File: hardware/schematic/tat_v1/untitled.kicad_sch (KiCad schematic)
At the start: 30 parts, among them J1 JST-PH 2 Pin, J2 USB_C_Receptacle_USB2.0_14P, SW1 SW_SPDT, U1 BQ25185, U2 USBLC6-2P6, U3 TPS631000DRLR

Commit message: Finished all footprints, can now start laying out circuit
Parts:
- F1: footprint (none) -> tat_footprints:Littelfuse_0805L_Polyfuse
- J1: footprint (none) -> Connector_JST:JST_PH_S2B-PH-SM4-TB_1x02-1MP_P2.00mm_Horizontal; Link (none) -> https://www.lcsc.com/product-detail/Wire-To-Board-Connector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
- SW1: footprint (none) -> tat_footprints:SW_SPDT_HANXIA_Mini_MSK12CO2; Link (none) -> https://www.lcsc.com/product-detail/Slide-Switches_SHOU-HAN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
- U1: footprint (none) -> tat_footprints:WSON-10 BQ25185
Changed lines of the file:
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@@
 			)
 		)
-		(property "Footprint" ""
+		(property "Footprint" "tat_footprints:WSON-10 BQ25185"
 			(at 74.93 146.05 0)
 			(effects
@@
 			)
 		)
-		(property "Footprint" ""
+		(property "Footprint" "tat_footprints:SW_SPDT_HANXIA_Mini_MSK12CO2"
 			(at 212.09 142.24 0)
 			(effects
@@
 			)
 		)
-		(property "Datasheet" "~"
+		(property "Datasheet" "https://www.lcsc.com/datasheet/lcsc_datasheet_2407161403_SHOU-HAN-MINI-MSK12CO2_C2681570.pdf"
 			(at 212.09 134.62 0)
 			(effects
@@
 		)
 		(property "Description" "Switch, single pole double throw"
+			(at 212.09 142.24 0)
+			(effects
+				(font
+					(size 1.27 1.27)
+				)
+				(hide yes)
+			)
+		)
+		(property "Link" "https://www.lcsc.com/product-detail/Slide-Switches_SHOU-HAN-MINI-MSK12CO2_C2681570.html"
 			(at 212.09 142.24 0)
 			(effects
@@
 			)
 		)
-		(property "Footprint" ""
+		(property "Footprint" "tat_footprints:Littelfuse_0805L_Polyfuse"
 			(at 170.18 43.18 0)
 			(effects
@@
 			)
 		)
-		(property "Footprint" ""
+		(property "Footprint" "Connector_JST:JST_PH_S2B-PH-SM4-TB_1x02-1MP_P2.00mm_Horizontal"
 			(at 30.48 120.65 0)
 			(effects
@@
 			)
 		)
-		(property "Datasheet" "~"
+		(property "Datasheet" "https://www.lcsc.com/datasheet/lcsc_datasheet_2411192313_XUNPU-WAFER-PH2-0-2PWB_C3029440.pdf"
 			(at 30.48 120.65 0)
 			(effects
@@
 			)
 		)
-		(property "Description" "Generic connector, single row, 01x02, script generated"
+		(property "Description" "JST-PH 2-pin surface mount connector, right angle"
 			(at 30.48 120.65 0)
 			(effects
+				(font
+					(size 1.27 1.27)
+				)
+				(hide yes)
+			)
+		)
+		(property "Link" "https://www.lcsc.com/product-detail/Wire-To-Board-Connector_XUNPU-WAFER-PH2-0-2PWB_C3029440.html?s_z=n_XUNPU%2520WAFER-PH2.0-2PWB"
+			(at 30.48 120.65 0)
+			(effects

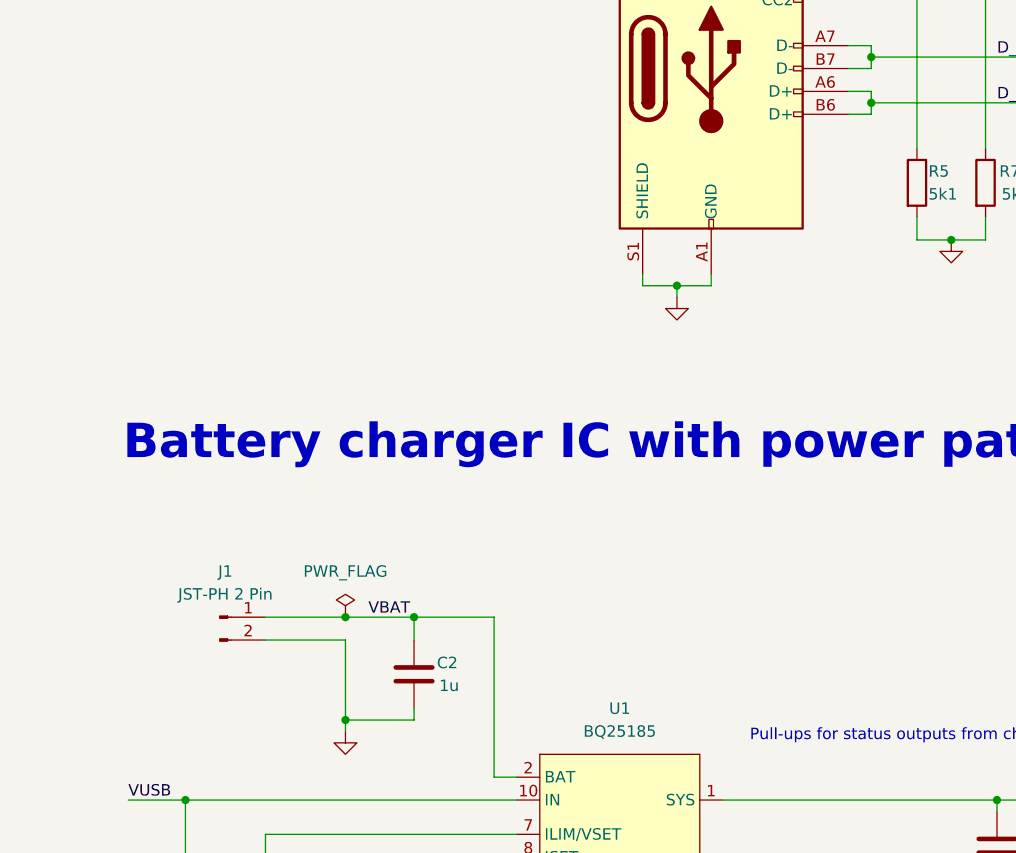
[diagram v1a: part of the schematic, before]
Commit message: Fixed all footprint-symbol mismatches, ready to start routing!
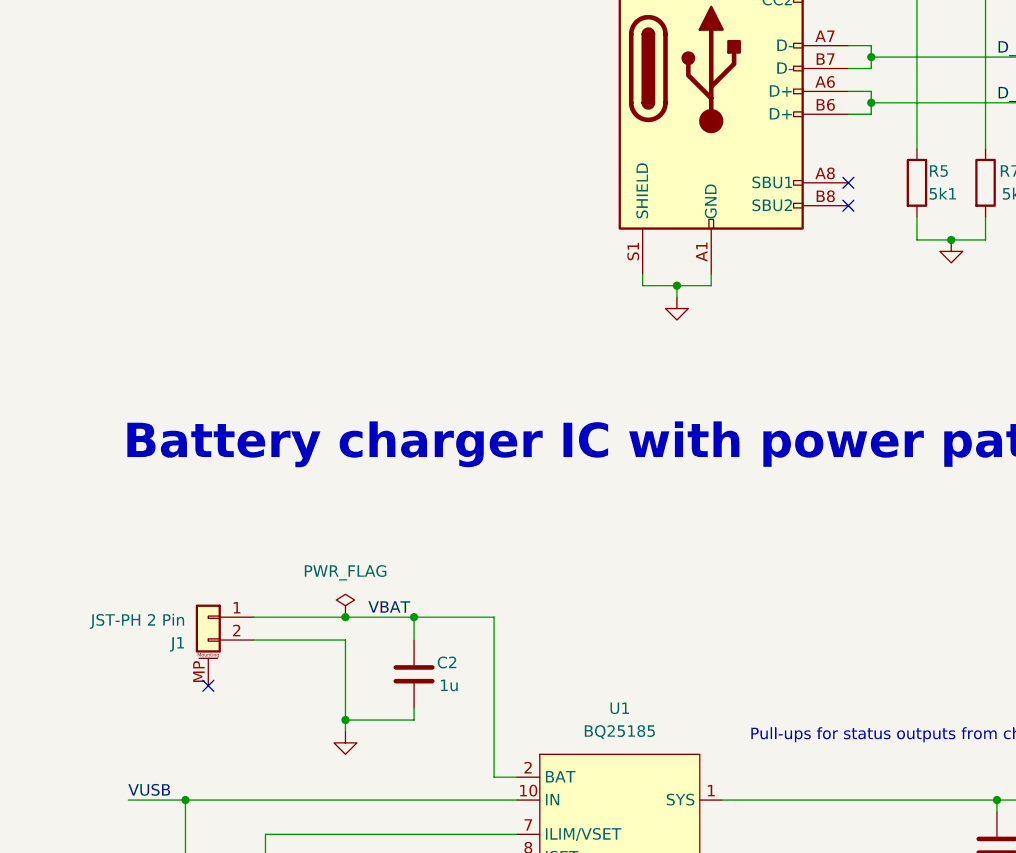
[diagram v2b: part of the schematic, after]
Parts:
- J1: symbol Connector:Conn_01x02_Pin -> Connector_Generic_MountingPin:Conn_01x02_MountingPin
- J2: symbol Connector:USB_C_Receptacle_USB2.0_14P -> Connector:USB_C_Receptacle_USB2.0_16P
- SW1: symbol Switch:SW_SPDT -> tat_library:MINI_MSK12CO2; Link https://www.lcsc.com/product-detail/Slide-Switches_SHOU-HAN-MINI-MSK12CO2_C2681570.html -> https://www.lcsc.com/product-detail/Slide-Switches_SHOU-HAN-MINI-MSK12CO2_C2681570.html?s_z=n_SHOU%2520HAN%2520MINI%2520MSK12CO2
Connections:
- no-connect marks 0 -> 3
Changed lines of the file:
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@@
 	)
 	(junction
+		(at 44.45 120.65)
+		(diameter 0)
+		(color 0 0 0 0)
+	)
+	(junction
 		(at 35.56 161.29)
 		(diameter 0)
@@
 	)
 	(junction
-		(at 44.45 120.65)
-		(diameter 0)
-		(color 0 0 0 0)
-	)
-	(junction
 		(at 44.45 132.08)
 		(diameter 0)
@@
 		(color 0 0 0 0)
 	)
+	(no_connect
+		(at 100.33 72.39)
+	)
+	(no_connect
+		(at 29.21 128.27)
+	)
+	(no_connect
+		(at 100.33 74.93)
+	)
 	(wire
 		(pts
@@
 	(wire
 		(pts
-			(xy 35.56 123.19) (xy 44.45 123.19)
-		)
-		(stroke
-			(width 0)
-			(type default)
-		)
-	)
-	(wire
-		(pts
 			(xy 134.62 62.23) (xy 137.16 62.23)
 		)
@@
 	(wire
 		(pts
-			(xy 35.56 120.65) (xy 44.45 120.65)
-		)
-		(stroke
-			(width 0)
-			(type default)
-		)
-	)
-	(wire
-		(pts
 			(xy 115.57 49.53) (xy 115.57 68.58)
 		)
@@
 	(wire
 		(pts
+			(xy 34.29 123.19) (xy 44.45 123.19)
+		)
+		(stroke
+			(width 0)
+			(type default)
+		)
+	)
+	(wire
+		(pts
 			(xy 26.67 161.29) (xy 35.56 161.29)
 		)
@@
 	(wire
 		(pts
+			(xy 34.29 120.65) (xy 44.45 120.65)
+		)
+		(stroke
+			(width 0)
+			(type default)
+		)
+	)
+	(wire
+		(pts
 			(xy 156.21 55.88) (xy 156.21 54.61)
 		)
@@
 	)
 	(symbol
-		(lib_id "Connector:USB_C_Receptacle_USB2.0_14P")
+		(lib_id "Connector:USB_C_Receptacle_USB2.0_16P")
 		(at 85.09 59.69 0)
 		(unit 1)
@@
 			)
 		)
-		(property "Datasheet" "https://www.lcsc.com/datasheet/lcsc_datasheet_2410010003_Korean-Hroparts-Elec-TYPE-C-31-M-12_C165948.pdf"
+		(property "Datasheet" "https://www.usb.org/sites/default/files/documents/usb_type-c.zip"
 			(at 88.9 59.69 0)
 			(effects
@@
 			)
 		)
-		(property "Description" "USB 2.0-only 14P Korean Hroparts Elec TYPE-C-31-M-12 Type-C Receptacle connector"
+		(property "Description" "USB 2.0-only 16P Type-C Receptacle connector"
 			(at 85.09 59.69 0)
 			(effects
@@
 		(pin "A1"
 		)
+		(pin "A8"
+		)
+		(pin "B8"
+		)
 		(instances
 			(project ""
@@
 	)
 	(symbol
-		(lib_id "Switch:SW_SPDT")
+		(lib_id "tat_library:MINI_MSK12CO2")
 		(at 212.09 142.24 180)
 		(unit 1)
@@
 		)
 		(property "Datasheet" "https://www.lcsc.com/datasheet/lcsc_datasheet_2407161403_SHOU-HAN-MINI-MSK12CO2_C2681570.pdf"
-			(at 212.09 134.62 0)
+			(at 212.09 134.366 0)
 			(effects
 				(font
@@
 			)
 		)
-		(property "Link" "https://www.lcsc.com/product-detail/Slide-Switches_SHOU-HAN-MINI-MSK12CO2_C2681570.html"
+		(property "Link" "https://www.lcsc.com/product-detail/Slide-Switches_SHOU-HAN-MINI-MSK12CO2_C2681570.html?s_z=n_SHOU%2520HAN%2520MINI%2520MSK12CO2"
 			(at 212.09 142.24 0)
 			(effects
@@
 		(pin "3"
 		)
+		(pin "4"
+		)
+		(pin "6"
+		)
+		(pin "7"
+		)
+		(pin "5"
+		)
 		(instances
 			(project ""
@@
 	)
 	(symbol
-		(lib_id "Connector:Conn_01x02_Pin")
-		(at 30.48 120.65 0)
+		(lib_id "Connector_Generic_MountingPin:Conn_01x02_MountingPin")
+		(at 29.21 120.65 0)
+		(mirror y)
 		(unit 1)
 		(exclude_from_sim no)
@@
 		(on_board yes)
 		(dnp no)
-		(fields_autoplaced yes)
 		(property "Reference" "J1"
-			(at 31.115 115.57 0)
+			(at 26.67 123.5457 0)
 			(effects
 				(font
 					(size 1.27 1.27)
 				)
+				(justify left)
 			)
 		)
 		(property "Value" "JST-PH 2 Pin"
-			(at 31.115 118.11 0)
+			(at 26.67 121.0057 0)
 			(effects
 				(font
 					(size 1.27 1.27)
 				)
+				(justify left)
 			)
 		)
 		(property "Footprint" "Connector_JST:JST_PH_S2B-PH-SM4-TB_1x02-1MP_P2.00mm_Horizontal"
-			(at 30.48 120.65 0)
+			(at 29.21 120.65 0)
 			(effects
 				(font
@@
 			)
 		)
-		(property "Datasheet" "https://www.lcsc.com/datasheet/lcsc_datasheet_2411192313_XUNPU-WAFER-PH2-0-2PWB_C3029440.pdf"
-			(at 30.48 120.65 0)
+		(property "Datasheet" "~"
+			(at 29.21 120.65 0)
 			(effects
 				(font
@@
 			)
 		)
-		(property "Description" "JST-PH 2-pin surface mount connector, right angle"
-			(at 30.48 120.65 0)
+		(property "Description" "Generic connectable mounting pin connector, single row, 01x02, script generated (kicad-library-utils/schlib/autogen/connector/)"
+			(at 29.21 120.65 0)
 			(effects
 				(font
@@
 		)
 		(property "Link" "https://www.lcsc.com/product-detail/Wire-To-Board-Connector_XUNPU-WAFER-PH2-0-2PWB_C3029440.html?s_z=n_XUNPU%2520WAFER-PH2.0-2PWB"
-			(at 30.48 120.65 0)
+			(at 29.21 120.65 0)
 			(effects
 				(font
@@
 		(pin "2"
 		)
+		(pin "MP"
+		)
 		(instances
